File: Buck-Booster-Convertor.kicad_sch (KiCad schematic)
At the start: 0 parts

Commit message: Added 4 FETS, 1 Inductor, 4 Resistors.
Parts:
- added L1: L, symbol Device:L
- added Q1, Q2, Q3, Q4: CSD18512Q5B, symbol Simulation_SPICE:NMOS
- added R1, R2, R3, R4: R_US, symbol Device:R_US
- added U1: (no value), symbol My-Library:LM5145

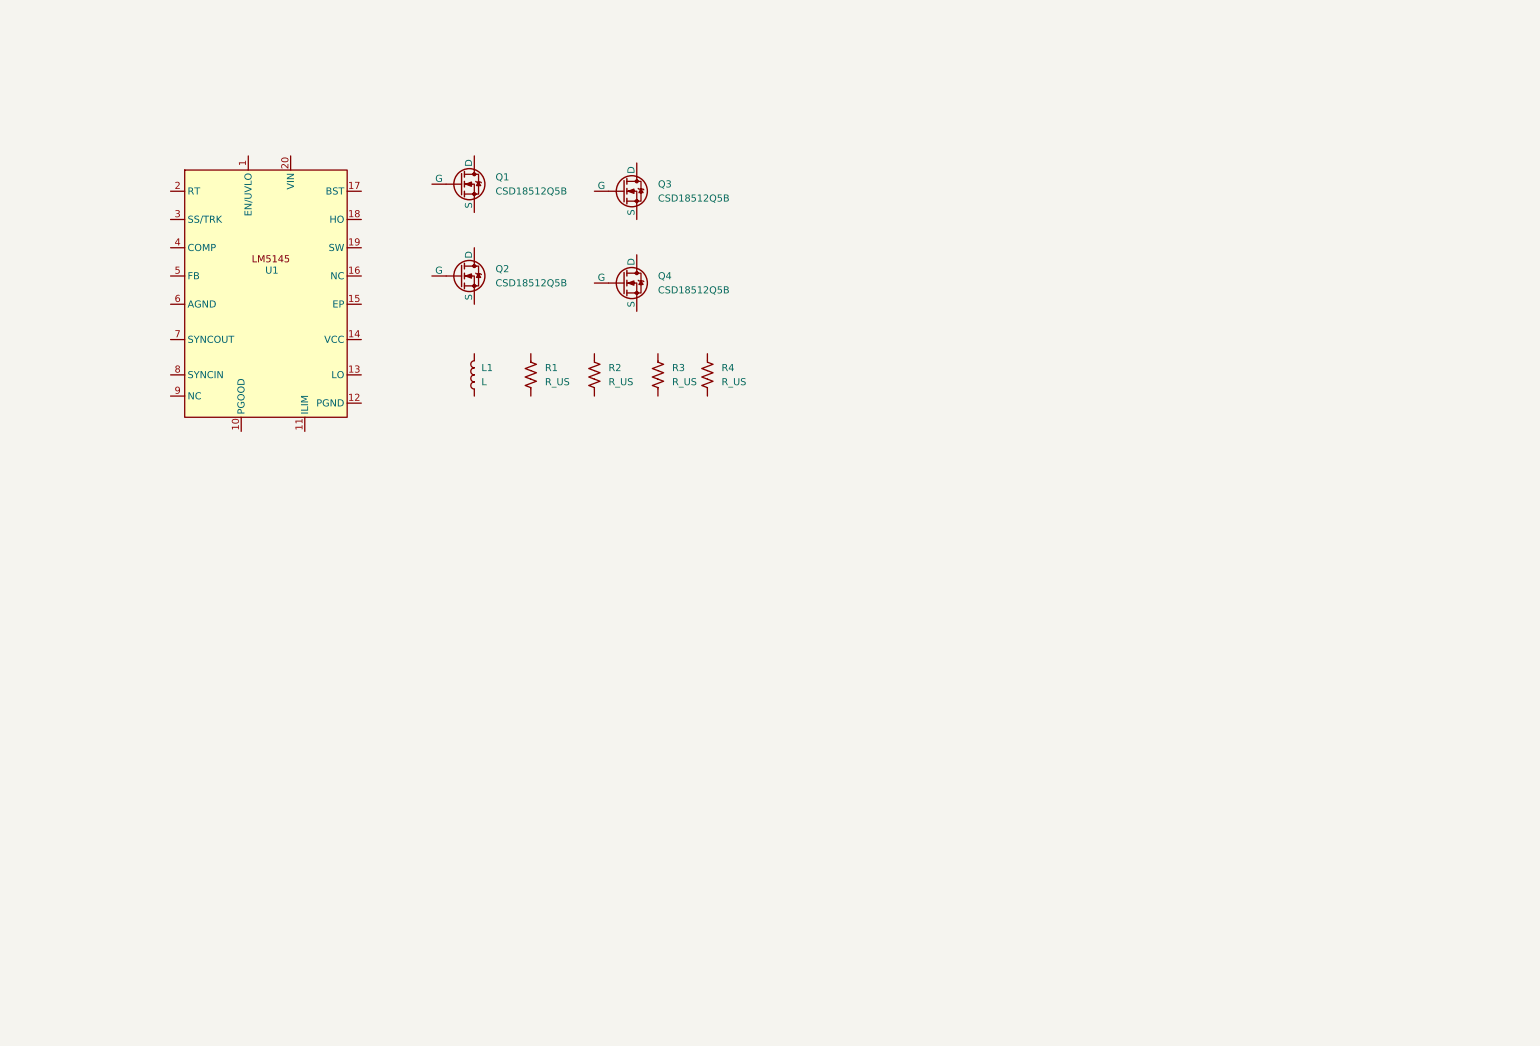
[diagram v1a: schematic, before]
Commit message: Expand schematic: add diodes, connectors, fuse, capacitors and resistors
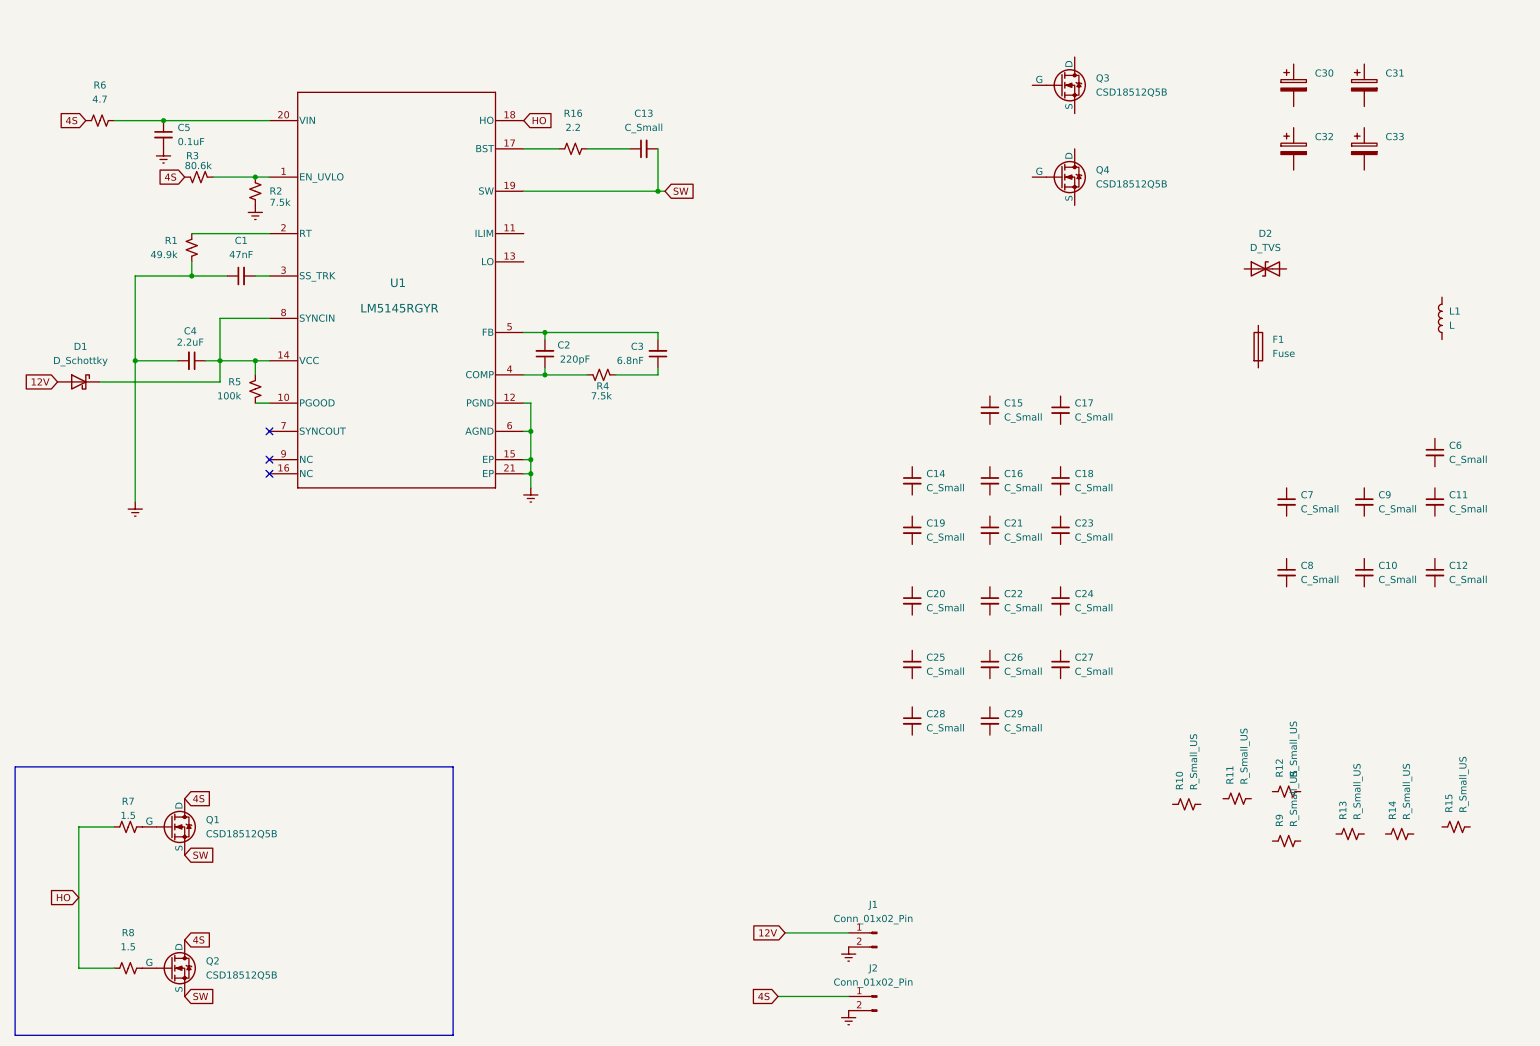
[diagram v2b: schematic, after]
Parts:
- removed R1, R2, R3, R4: R_US, symbol Device:R_US
- removed U1: (no value), symbol My-Library:LM5145
- added C1: 47nF, symbol Device:C_Small
- added C10, C11, C12, C13, C14, C15, C16, C17, C18, C19, C20, C21, C22, C23, C24, C25, C26, C27, C28, C29, C6, C7, C8, C9: C_Small, symbol Device:C_Small
- added C2: 220pF, symbol Device:C_Small
- added C3: 6.8nF, symbol Device:C_Small
- added C30, C31, C32, C33: C_Polarized, symbol Device:C_Polarized
- added C4: 2.2uF, symbol Device:C_Small
- added C5: 0.1uF, symbol Device:C_Small
- added D1: D_Schottky, symbol Device:D_Schottky
- added D2: D_TVS, symbol Device:D_TVS
- added F1: Fuse, symbol Device:Fuse
- added J1, J2: Conn_01x02_Pin, symbol Connector:Conn_01x02_Pin
- added R1: 49.9k, symbol Device:R_Small_US
- added R10, R11, R12, R13, R14, R15, R9: R_Small_US, symbol Device:R_Small_US
- added R16: 2.2, symbol Device:R_Small_US
- added R2, R4: 7.5k, symbol Device:R_Small_US
- added R3: 80.6k, symbol Device:R_Small_US
- added R5: 100k, symbol Device:R_Small_US
- added R6: 4.7, symbol Device:R_Small_US
- added R7, R8: 1.5, symbol Device:R_Small_US
- added U1: LM5145RGYR, RGY0020B, symbol My-Library:LM5145RGYR
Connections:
- net 4S: now reaches Q2.1 (D)
- net 4S: now also Q1.1 (D), J2.1 (Pin_1), R3.2, R6.1
- net at Q2.2 (G): now also R8.2
- net SW: now reaches Q2.3 (S)
- net SW: now also Q1.3 (S), C13.2, U1.19 (SW)
- net at Q1.2 (G): now also R7.2
- new net: C4.1, D1.1 (K), R5.1, U1.14 (VCC), U1.8 (SYNCIN)
- new net: R2.2, R3.1, U1.1 (EN_UVLO)
- new net: R5.2, U1.10 (PGOOD)
- new net: C1.2, U1.3 (SS_TRK)
- new net: C3.1, R4.2
- new net: C2.2, C3.2, U1.5 (FB)
- new net: R1.1, U1.2 (RT)
- new net: C5.1, R6.2, U1.20 (VIN)
- new net: C2.1, R4.1, U1.4 (COMP)
- new net: R16.1, U1.17 (BST)
- new net: C13.1, R16.2
- new net 12V: D1.2 (A), J1.1 (Pin_1)
- new net GNDREF: C1.1, C4.2, C5.2, J1.2 (Pin_2), J2.2 (Pin_2), R1.2, R2.1, U1.12 (PGND), U1.15 (EP), U1.21 (EP), U1.6 (AGND)
- new net HO: R7.1, R8.1, U1.18 (HO)
- no-connect marks 0 -> 3
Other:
- moved on the sheet: L1, Q1, Q2, Q3, Q4

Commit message: Update schematic: add D3, J3 and power symbols
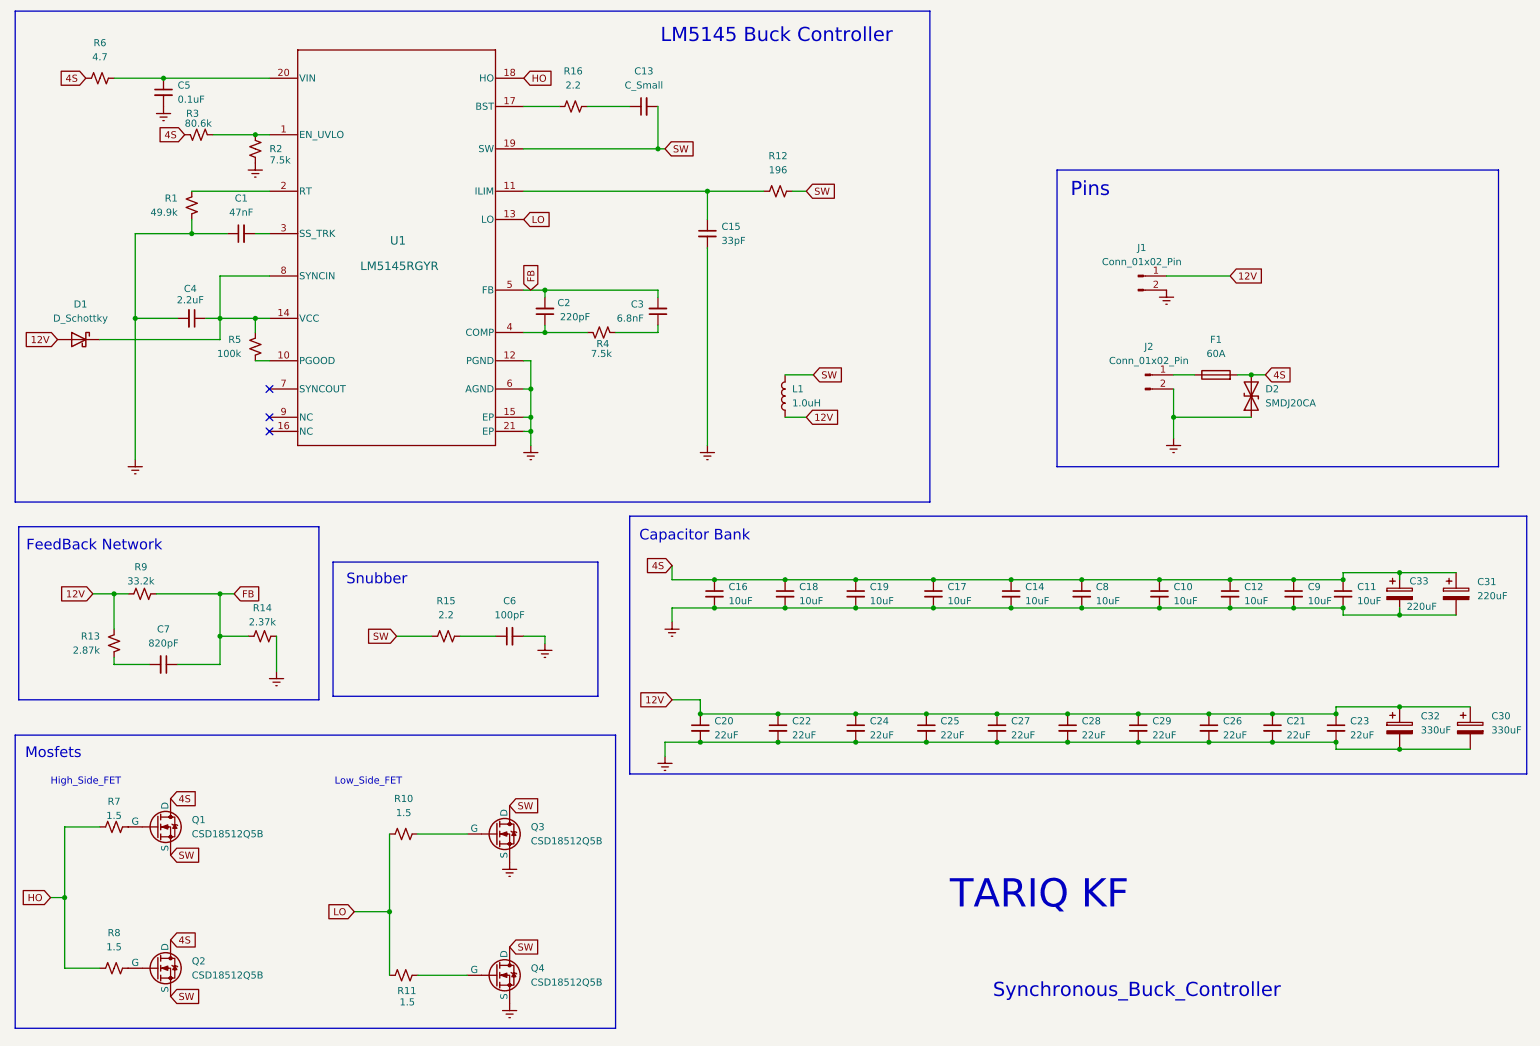
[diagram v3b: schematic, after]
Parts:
- C10, C11, C12, C14, C16, C17, C18, C19, C8, C9: value C_Small -> 10uF
- C15: value C_Small -> 33pF
- C20, C21, C22, C23, C24, C25, C26, C27, C28, C29: value C_Small -> 22uF
- C30, C32: value C_Polarized -> 330uF
- C31, C33: value C_Polarized -> 220uF
- C6: value C_Small -> 100pF
- C7: value C_Small -> 820pF
- D2: value D_TVS -> SMDJ20CA
- F1: value Fuse -> 60A
- L1: value L -> 1.0uH
- R10, R11: value R_Small_US -> 1.5
- R12: value R_Small_US -> 196
- R13: value R_Small_US -> 2.87k
- R14: value R_Small_US -> 2.37k
- R15: value R_Small_US -> 2.2
- R9: value R_Small_US -> 33.2k
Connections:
- net 12V: now also C20.1, C21.1, C22.1, C23.1, C24.1, C25.1, C26.1, C27.1, C28.1, C29.1, C30.1, C32.1, L1.1, R13.2, R9.1
- net 4S: now also C10.1, C11.1, C12.1, C14.1, C16.1, C17.1, C18.1, C19.1, C31.1, C33.1, C8.1, C9.1, D2.2 (A2), F1.2; no longer J2.1 (Pin_1)
- net GNDREF: now also C10.2, C11.2, C12.2, C14.2, C15.2, C16.2, C17.2, C18.2, C19.2, C20.2, C21.2, C22.2, C23.2, C24.2, C25.2, C26.2, C27.2, C28.2, C29.2, C30.2, C31.2, C32.2, C33.2, C6.2, C8.2, C9.2, D2.1 (A1), Q3.3 (S), Q4.3 (S), R14.2
- net SW: now also L1.2, Q3.1 (D), Q4.1 (D), R12.2, R15.1
- net at R12.1: now also C15.1, U1.11 (ILIM)
- net at Q4.2 (G): now also R11.2
- net at F1.1: now also J2.1 (Pin_1)
- net at R15.2: now also C6.1
- net LO: now reaches R10.1
- net LO: now also R11.1, U1.13 (LO)
- net at R10.2: now also Q3.2 (G)
- net FB: now reaches C7.1
- net FB: now also C2.2, C3.2, R14.1, R9.2, U1.5 (FB)
- net at C7.2: now also R13.1
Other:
- note added: "Capacitor Bank"
- note added: "FeedBack Network"
- note added: "High_Side_FET"
- note added: "LM5145 Buck Controller"
- note added: "Low_Side_FET"
- note added: "Mosfets"
- note added: "Pins"
- note added: "Snubber"
- note added: "Synchronous_Buck_Controller"
- note added: "TARIQ KF"
- moved on the sheet: C1, C10, C11, C12, C13, C14, C15, C16, C17, C18, C19, C2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
